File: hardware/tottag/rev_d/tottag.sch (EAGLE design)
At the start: 142 parts, among them J1 BAT_HOLE, J2 CON_MICRO_SDDM3AT-SF-PEJM5, J3 MICRO_USB_B_HIROSE_ZX62-B-5PA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, J4 TC2030-JLINK-NL, J5 TC2030-JLINK-NL, T1 HHM1595A1, U1 DW1000, U10 STM32F091CC, U2 FT232RQ, U3 LIS2DW12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

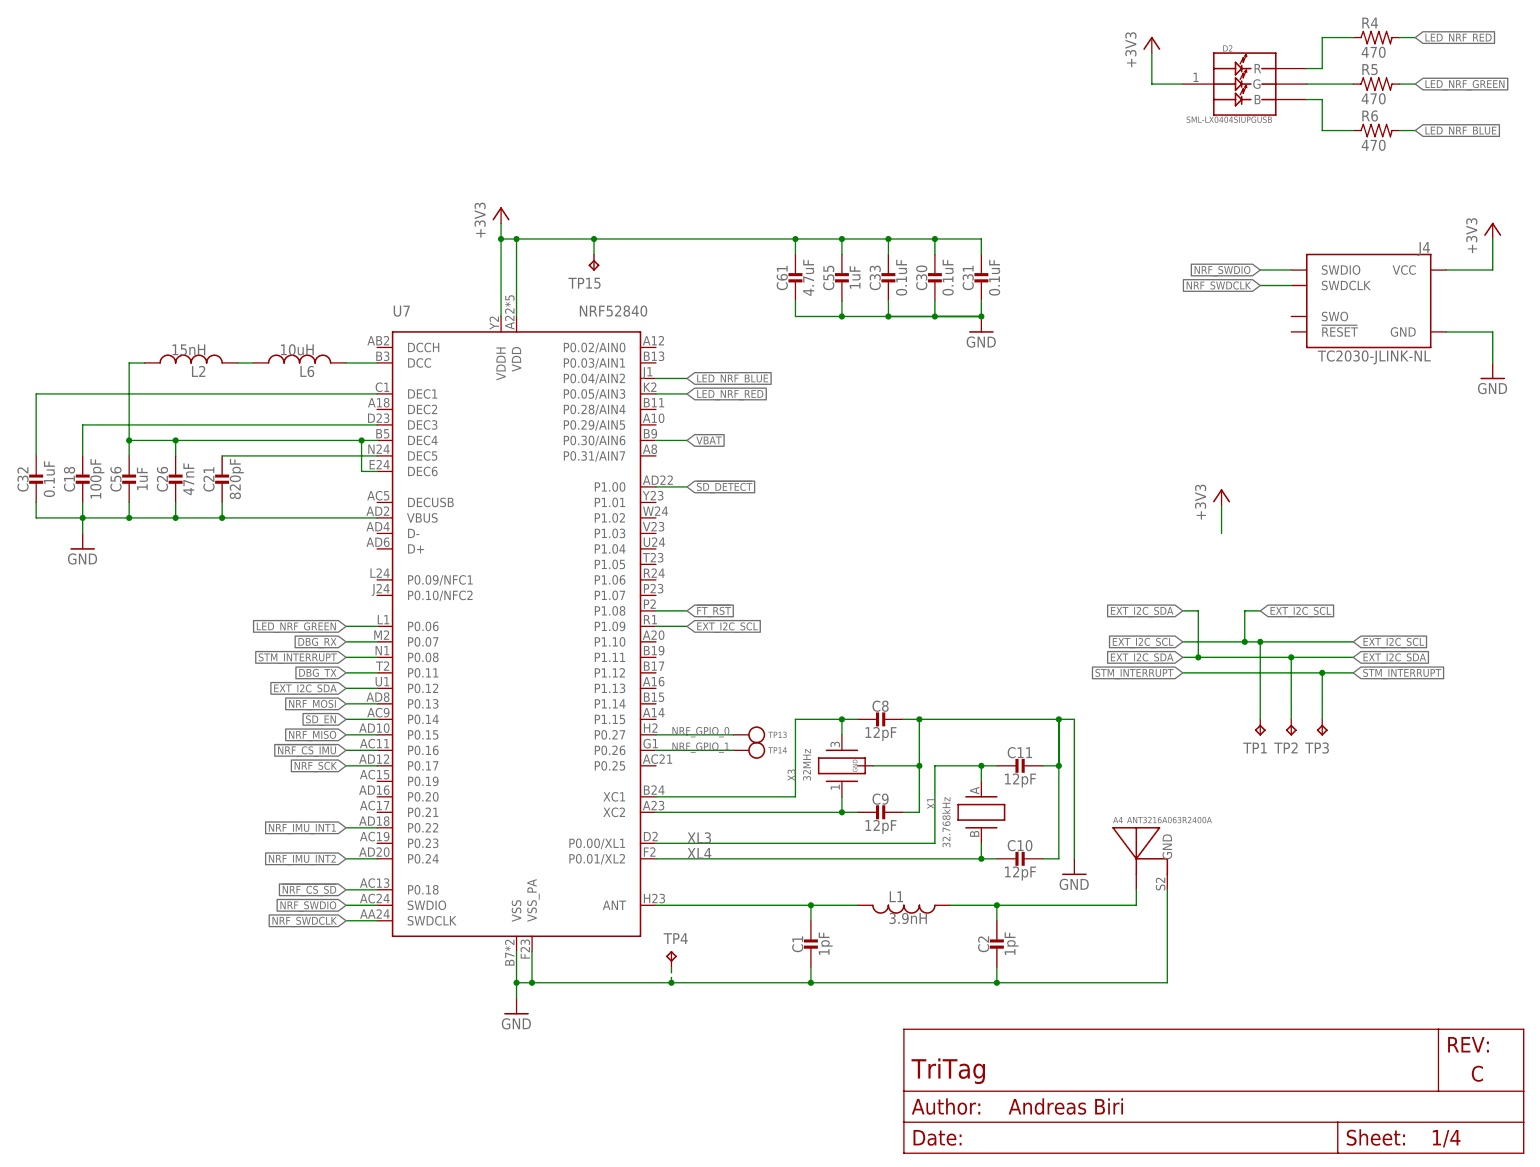
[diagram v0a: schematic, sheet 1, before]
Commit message: added connection to RST pin of nRF
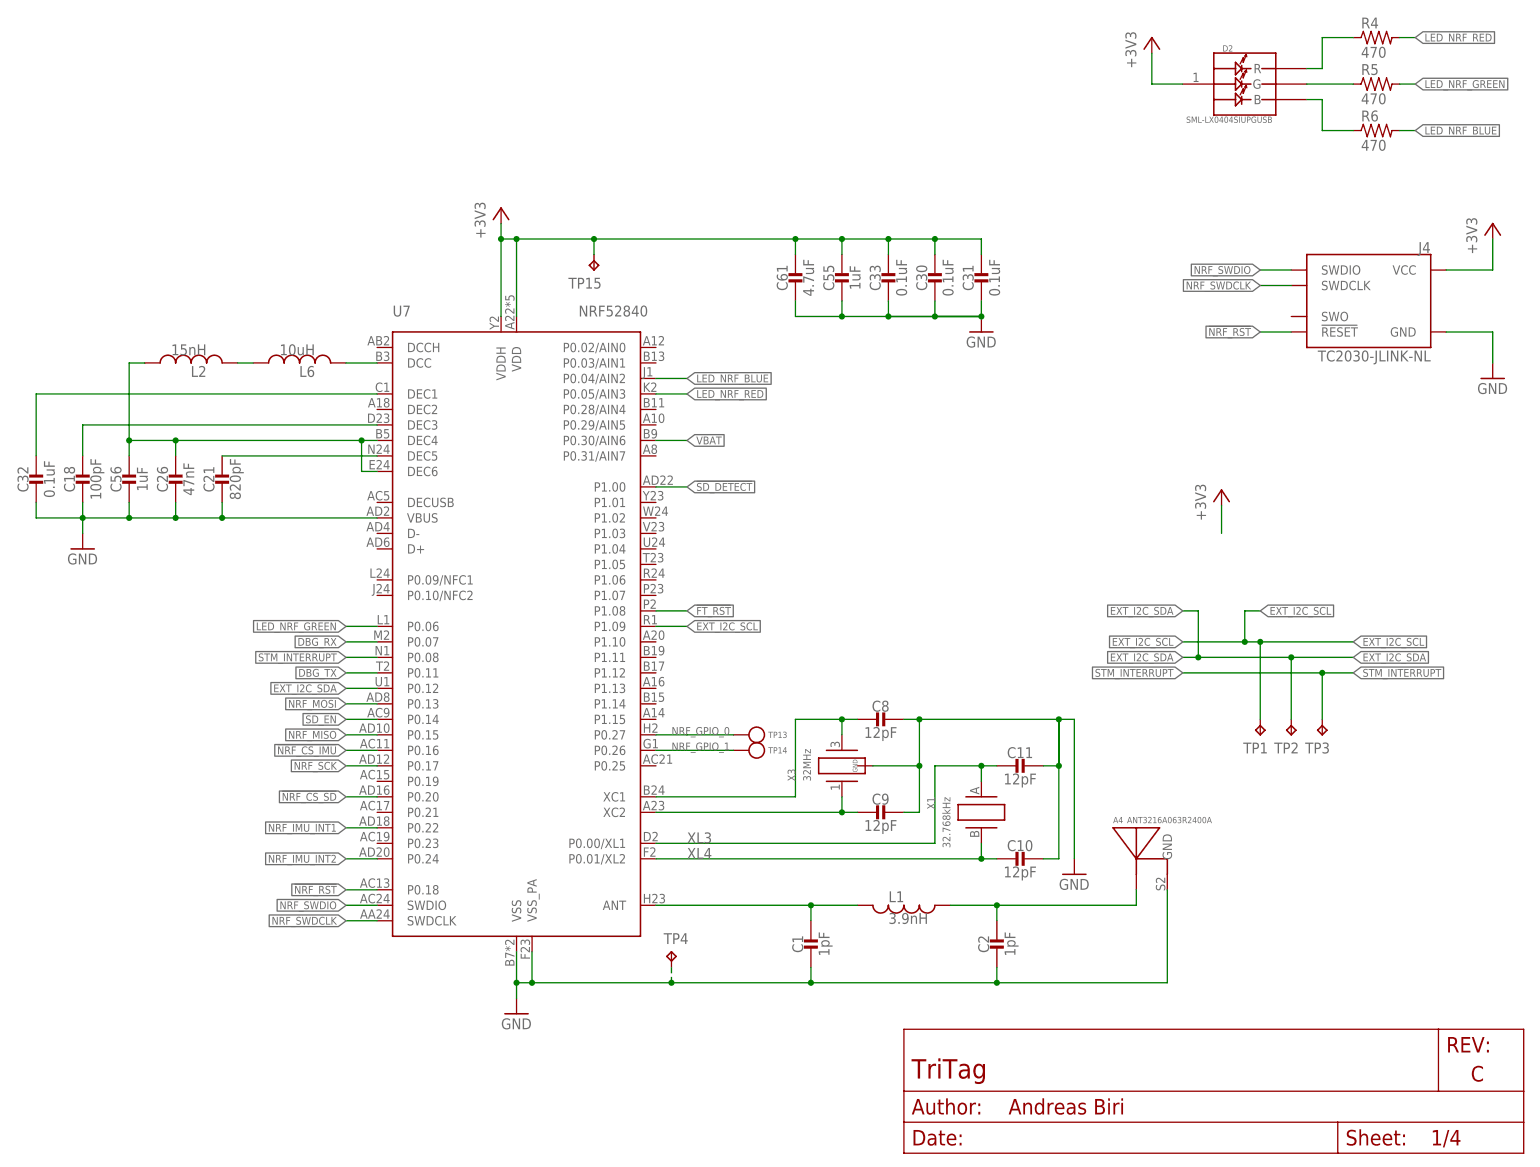
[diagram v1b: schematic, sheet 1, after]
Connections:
- new net !NRF_RST: J4.!RESET, U7.P0.18
- net !NRF_CS_SD: now also U7.P0.20; no longer U7.P0.18
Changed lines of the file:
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@@
-</segment>
-</net>
-<net name="!NRF_CS_SD" class="0">
-<segment>
-<pinref part="U7" gate="G$1" pin="P0.18"/>
-<wire x1="60.96" y1="43.18" x2="55.88" y2="43.18" width="0.1524" layer="91"/>
-<label x="55.88" y="43.18" size="1.27" layer="95" rot="R180" xref="yes"/>
 </segment>
 </net>
@@
 </segment>
 </net>
+<net name="!NRF_CS_SD" class="0">
+<segment>
+<pinref part="U7" gate="G$1" pin="P0.20"/>
+<wire x1="60.96" y1="58.42" x2="55.88" y2="58.42" width="0.1524" layer="91"/>
+<label x="55.88" y="58.42" size="1.27" layer="95" rot="R180" xref="yes"/>
+</segment>
+</net>
+<net name="!NRF_RST" class="0">
+<segment>
+<pinref part="U7" gate="G$1" pin="P0.18"/>
+<wire x1="60.96" y1="43.18" x2="55.88" y2="43.18" width="0.1524" layer="91"/>
+<label x="55.88" y="43.18" size="1.27" layer="95" rot="R180" xref="yes"/>
+</segment>
+<segment>
+<pinref part="J4" gate="G$1" pin="!RESET"/>
+<wire x1="210.82" y1="134.62" x2="205.74" y2="134.62" width="0.1524" layer="91"/>
+<label x="205.74" y="134.62" size="1.27" layer="95" rot="R180" xref="yes"/>
+</segment>
+</net>

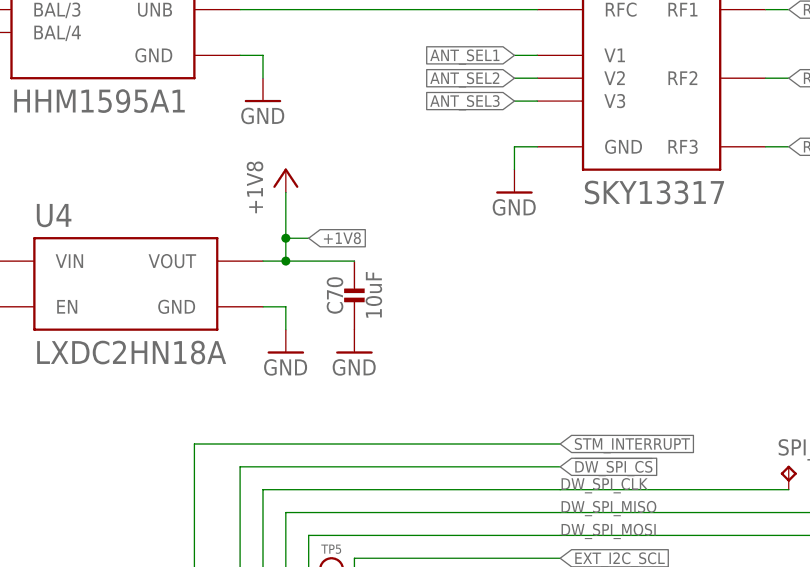
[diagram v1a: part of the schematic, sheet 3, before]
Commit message: added testpoint for +1V8, optimized power plane, added ground vias, shifted test pads
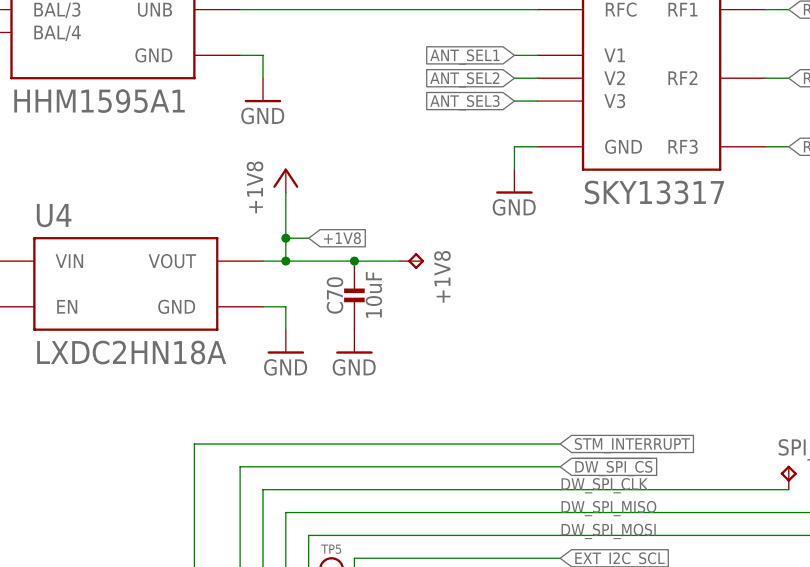
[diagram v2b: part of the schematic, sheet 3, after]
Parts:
- added +1V8: TPTP06SQ, testpad:TPTP06SQ
- J1: value BAT_HOLE -> MICRO_USB_B_HIROSE_ZX62-B-5PA(11); device connector:BAT_HOLE -> connector:MICRO_USB_B_HIROSE_ZX62-B-5PA(11)
- J3: value MICRO_USB_B_HIROSE_ZX62-B-5PA(11) -> BAT_HOLE; device connector:MICRO_USB_B_HIROSE_ZX62-B-5PA(11) -> connector:BAT_HOLE
- renumbered L6 to L3
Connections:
- net +1V8: now also +1V8.TP
- net D+: now also J1.D+; no longer J3.D+
- net D-: now also J1.D-; no longer J3.D-
- net GND: now also J1.GND, J3.-; no longer J1.-, J3.GND
- net VBAT: now also J3.+; no longer J1.+
- net VUSB: now also J1.+5V; no longer J3.+5V
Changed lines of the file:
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@@
 <part name="D1" library="SparkFun-LED" deviceset="LED" device="0603" value="GREEN"/>
 <part name="SUPPLY2" library="supply1" library_urn="urn:adsk.eagle:library:371" deviceset="GND" device=""/>
-<part name="J3" library="connector" deviceset="MICRO_USB_B_HIROSE_ZX62-B-5PA(11)" device=""/>
-<part name="J1" library="connector" deviceset="BAT_HOLE" device=""/>
+<part name="J1" library="connector" deviceset="MICRO_USB_B_HIROSE_ZX62-B-5PA(11)" device=""/>
+<part name="J3" library="connector" deviceset="BAT_HOLE" device=""/>
 <part name="SUPPLY8" library="supply1" library_urn="urn:adsk.eagle:library:371" deviceset="GND" device=""/>
 <part name="TP2" library="testpad" library_urn="urn:adsk.eagle:library:385" deviceset="TP" device="TP06SQ" package3d_urn="urn:adsk.eagle:package:27952/1"/>
@@
 <attribute name="MPN" value="HK100515NJ-T "/>
 </part>
-<part name="L6" library="passives" deviceset="INDUCTOR" device="0603" value="10uH">
+<part name="L3" library="passives" deviceset="INDUCTOR" device="0603" value="10uH">
 <attribute name="DIGIKEY" value="490-4025-1-ND"/>
 <attribute name="MPN" value="LQM18FN100M00D "/>
@@
 <part name="MISO" library="testpad" library_urn="urn:adsk.eagle:library:385" deviceset="TP" device="TP06SQ" package3d_urn="urn:adsk.eagle:package:27952/1"/>
 <part name="MOSI" library="testpad" library_urn="urn:adsk.eagle:library:385" deviceset="TP" device="TP06SQ" package3d_urn="urn:adsk.eagle:package:27952/1"/>
+<part name="+1V8" library="testpad" library_urn="urn:adsk.eagle:library:385" deviceset="TP" device="TP06SQ" package3d_urn="urn:adsk.eagle:package:27952/1"/>
 </parts>
 <sheets>
@@
 <attribute name="MPN" x="30.48" y="129.54" size="1.778" layer="96" rot="R90" display="off"/>
 </instance>
-<instance part="L6" gate="G$1" x="48.26" y="129.54" rot="R90">
+<instance part="L3" gate="G$1" x="48.26" y="129.54" rot="R90">
 <attribute name="DIGIKEY" x="48.26" y="129.54" size="1.778" layer="96" rot="R90" display="off"/>
 <attribute name="MPN" x="48.26" y="129.54" size="1.778" layer="96" rot="R90" display="off"/>
@@
 <pinref part="U7" gate="G$1" pin="DCC"/>
 <wire x1="55.88" y1="129.54" x2="60.96" y2="129.54" width="0.1524" layer="91"/>
-<pinref part="L6" gate="G$1" pin="2"/>
+<pinref part="L3" gate="G$1" pin="2"/>
 </segment>
 </net>
@@
 <pinref part="L2" gate="G$1" pin="2"/>
 <wire x1="40.64" y1="129.54" x2="38.1" y2="129.54" width="0.1524" layer="91"/>
-<pinref part="L6" gate="G$1" pin="1"/>
+<pinref part="L3" gate="G$1" pin="1"/>
 </segment>
 </net>
@@
 <instance part="D1" gate="G$1" x="76.2" y="149.86"/>
 <instance part="SUPPLY2" gate="1" x="142.24" y="127"/>
-<instance part="J3" gate="G$1" x="22.86" y="152.4" rot="MR0"/>
-<instance part="J1" gate="G$1" x="190.5" y="175.26" rot="MR0"/>
+<instance part="J1" gate="G$1" x="22.86" y="152.4" rot="MR0"/>
+<instance part="J3" gate="G$1" x="190.5" y="175.26" rot="MR0"/>
 <instance part="SUPPLY8" gate="1" x="177.8" y="165.1"/>
 <instance part="U5" gate="G$1" x="218.44" y="157.48"/>
@@
 <wire x1="35.56" y1="139.7" x2="43.18" y2="139.7" width="0.1524" layer="91"/>
 <junction x="43.18" y="139.7"/>
-<pinref part="J3" gate="G$1" pin="GND"/>
+<pinref part="J1" gate="G$1" pin="GND"/>
 <wire x1="30.48" y1="147.32" x2="35.56" y2="147.32" width="0.1524" layer="91"/>
 </segment>
@@
 <pinref part="SUPPLY8" gate="1" pin="GND"/>
 <wire x1="177.8" y1="167.64" x2="177.8" y2="172.72" width="0.1524" layer="91"/>
-<pinref part="J1" gate="G$1" pin="-"/>
+<pinref part="J3" gate="G$1" pin="-"/>
 <wire x1="177.8" y1="172.72" x2="180.34" y2="172.72" width="0.1524" layer="91"/>
 </segment>
@@
 <wire x1="63.5" y1="167.64" x2="76.2" y2="167.64" width="0.1524" layer="91"/>
 <wire x1="35.56" y1="167.64" x2="35.56" y2="157.48" width="0.1524" layer="91"/>
-<pinref part="J3" gate="G$1" pin="+5V"/>
+<pinref part="J1" gate="G$1" pin="+5V"/>
 <wire x1="35.56" y1="157.48" x2="30.48" y2="157.48" width="0.1524" layer="91"/>
 <pinref part="U6" gate="U1" pin="VDD/2"/>
@@
 <junction x="200.66" y="160.02"/>
 <wire x1="170.18" y1="177.8" x2="170.18" y2="160.02" width="0.1524" layer="91"/>
-<pinref part="J1" gate="G$1" pin="+"/>
+<pinref part="J3" gate="G$1" pin="+"/>
 <wire x1="170.18" y1="177.8" x2="180.34" y2="177.8" width="0.1524" layer="91"/>
 <pinref part="U5" gate="G$1" pin="IN"/>
@@
 </segment>
 <segment>
-<pinref part="J3" gate="G$1" pin="D-"/>
+<pinref part="J1" gate="G$1" pin="D-"/>
 <wire x1="30.48" y1="154.94" x2="35.56" y2="154.94" width="0.1524" layer="91"/>
 <label x="35.56" y="154.94" size="1.016" layer="95" xref="yes"/>
@@
 </segment>
 <segment>
-<pinref part="J3" gate="G$1" pin="D+"/>
+<pinref part="J1" gate="G$1" pin="D+"/>
 <wire x1="30.48" y1="152.4" x2="35.56" y2="152.4" width="0.1524" layer="91"/>
 <label x="35.56" y="152.4" size="1.016" layer="95" xref="yes"/>
@@
 <instance part="MISO" gate="G$1" x="124.46" y="127"/>
 <instance part="MOSI" gate="G$1" x="129.54" y="124.46"/>
+<instance part="+1V8" gate="G$1" x="78.74" y="152.4" rot="R270"/>
 </instances>
 <busses>
@@
 <wire x1="63.5" y1="154.94" x2="63.5" y2="160.02" width="0.1524" layer="91"/>
 <junction x="63.5" y="154.94"/>
-</segment>
-<segment>
+<pinref part="+1V8" gate="G$1" pin="TP"/>
+<wire x1="71.12" y1="152.4" x2="76.2" y2="152.4" width="0.1524" layer="91"/>
+<junction x="71.12" y="152.4"/>
+</segment>
+<segment>
